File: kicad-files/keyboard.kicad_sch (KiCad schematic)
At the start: 188 parts, among them J1 TYPE-C-31-M12_13, Q1 2N7002, Q2 2N7002, SW1 K2-1187SQ-A4SW-06, T1 53261-0471, T2 53261-0471, U1 STM32F411CEU6, U2 USBLC6-2SC6, U3 AT24C256C-SSHL-T, U4 SGM2007-3.3XN5/TR, Y1 TAXM8M4RFDCET2T

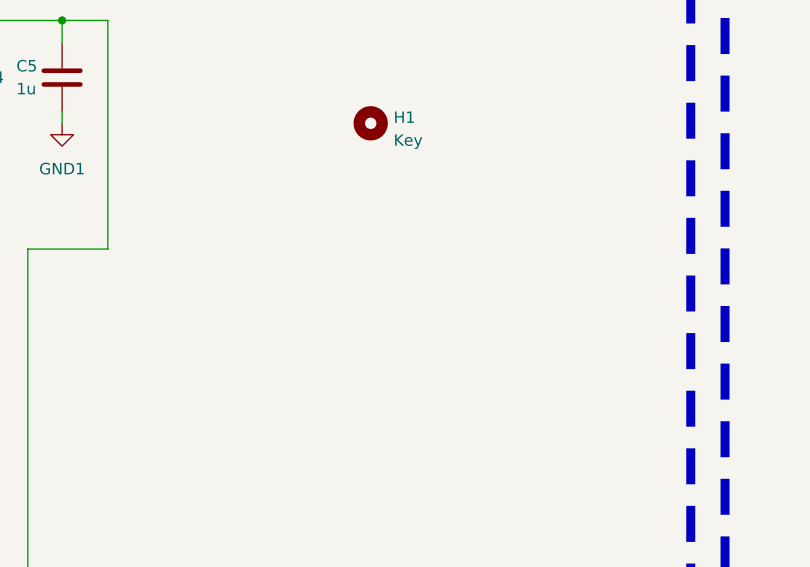
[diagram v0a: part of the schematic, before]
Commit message: Added legshark logo back
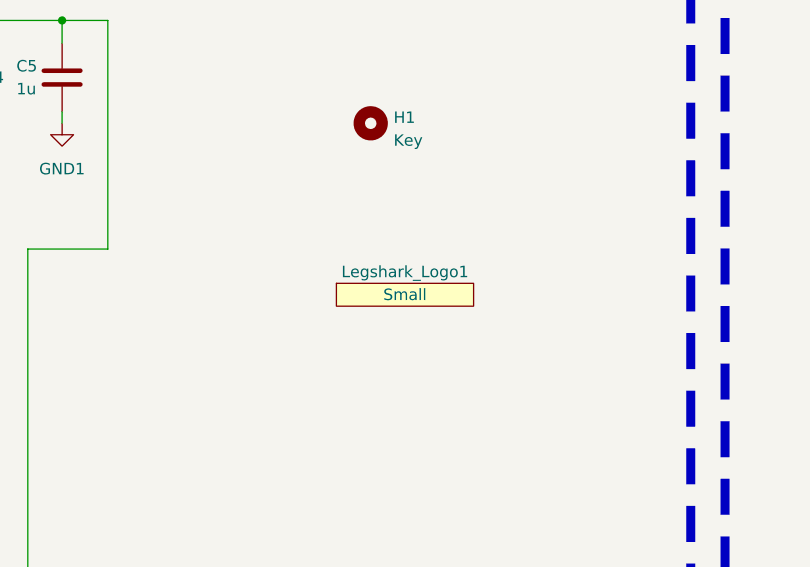
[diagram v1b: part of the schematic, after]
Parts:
- added Legshark_Logo1: Small, Legshark:Legshark_Logo_SMall, symbol legshark_symbols:Legshark_Logo
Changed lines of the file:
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@@
+    )
+  )
+  (symbol (lib_id "legshark_symbols:Legshark_Logo") (at 369.57 345.44 0) (unit 1)
+    (in_bom yes) (on_board yes) (dnp no) (fields_autoplaced)
+    (property "Reference" "Legshark_Logo1" (at 369.57 342.9 0)
+      (effects (font (size 1.27 1.27)))
+    )
+    (property "Value" "Small" (at 369.57 345.44 0)
+      (effects (font (size 1.27 1.27)))
+    )
+    (property "Footprint" "Legshark:Legshark_Logo_SMall" (at 369.57 345.44 0)
+      (effects (font (size 1.27 1.27)) hide)
+    )
+    (property "Datasheet" "" (at 369.57 345.44 0)
+      (effects (font (size 1.27 1.27)) hide)
+    )
+    (instances
+      (project "keyboard"
+        (path "/2fda2561-53ed-4930-8b41-858e0e3dd5f4"
+          (reference "Legshark_Logo1") (unit 1)
+        )
+      )
     )
   )

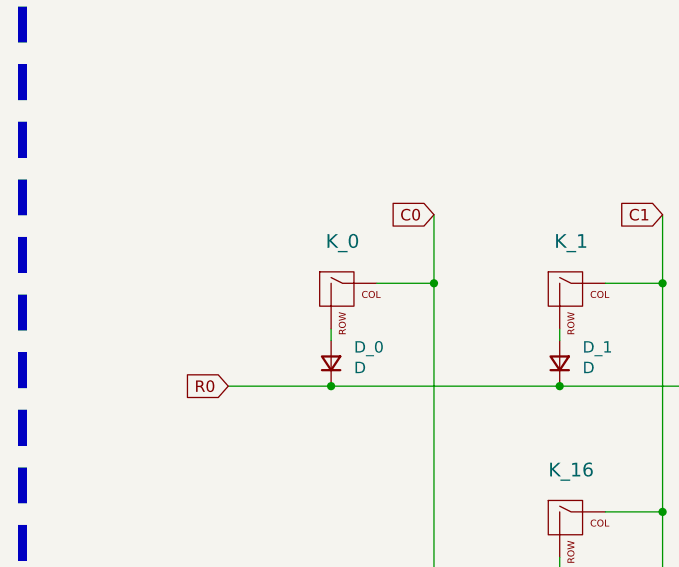
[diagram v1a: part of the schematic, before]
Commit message: Started naming the switches
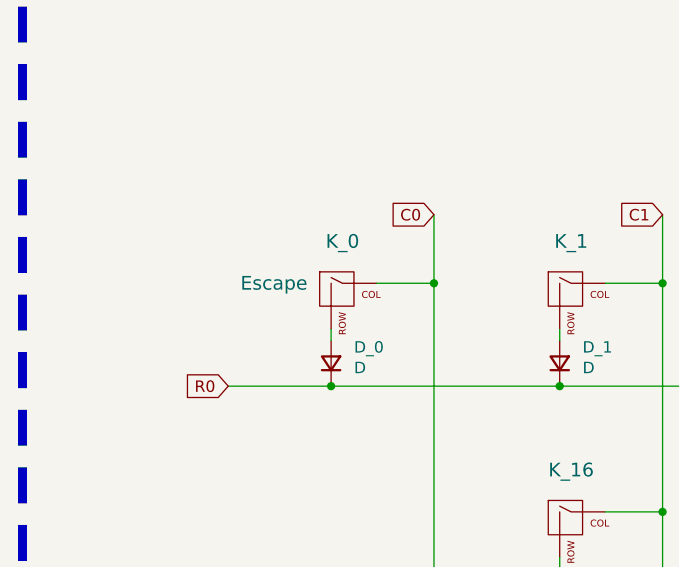
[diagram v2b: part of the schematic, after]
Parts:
- K_0: value KEYSW -> Escape
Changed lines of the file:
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@@
       (effects (font (size 1.524 1.524)))
     )
-    (property "Value" "KEYSW" (at 224.79 146.05 0)
-      (effects (font (size 1.524 1.524)) hide)
+    (property "Value" "Escape" (at 217.17 142.24 0)
+      (effects (font (size 1.524 1.524)))
     )
     (property "Footprint" "MX_Only:MXOnly-1U-NoLED" (at 224.79 143.51 0)

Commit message: Connected all of the columns
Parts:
- added C14: 100n, Capacitor_SMD:C_0603_1608Metric_Pad1.08x0.95mm_HandSolder, symbol Device:C
- added C15: 4.7u, Capacitor_SMD:C_0603_1608Metric_Pad1.08x0.95mm_HandSolder, symbol Device:C
- added C16: 16V 10uF Tantallum, acheron_Components:CP_EIA-3216-10_Kemet-I_Pad1.58x1.35mm_HandSolder, symbol Device:C_Polarized_US
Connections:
- net 3V3: now also U1.1 (VBAT), C14.1, C16.1
- net C0: now also U1.46 (PB9)
- net C1: now also U1.45 (PB8)
- net C10: now also U1.28 (PB15/SPI2_MOSI)
- net C11: now also U1.27 (PB14)
- net C12: now also U1.26 (PB13/SPI2_SCK)
- net C13: now also U1.25 (PB12)
- net C14: now also U1.21 (PB10)
- net C15: now also U1.19 (PB1)
- net C16: now also U1.18 (PB0)
- net C2: now also U1.41 (PB5)
- net C3: now also U1.40 (PB4)
- net C4: now also U1.39 (PB3)
- net C5: now also U1.38 (PA15)
- net C6: now also U1.37 (SWCLK/PA14)
- net C7: now also U1.34 (SWDIO/PA13)
- net C8: now also U1.31 (PA10)
- net C9: now also U1.29 (PA8)
- net GND: now also C14.2, C15.2, C16.2
- net at U1.22 (VCAP_1): now also C15.1
- no-connect marks 2 -> 3
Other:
- note added: "Scary pin that is internally pulled down"

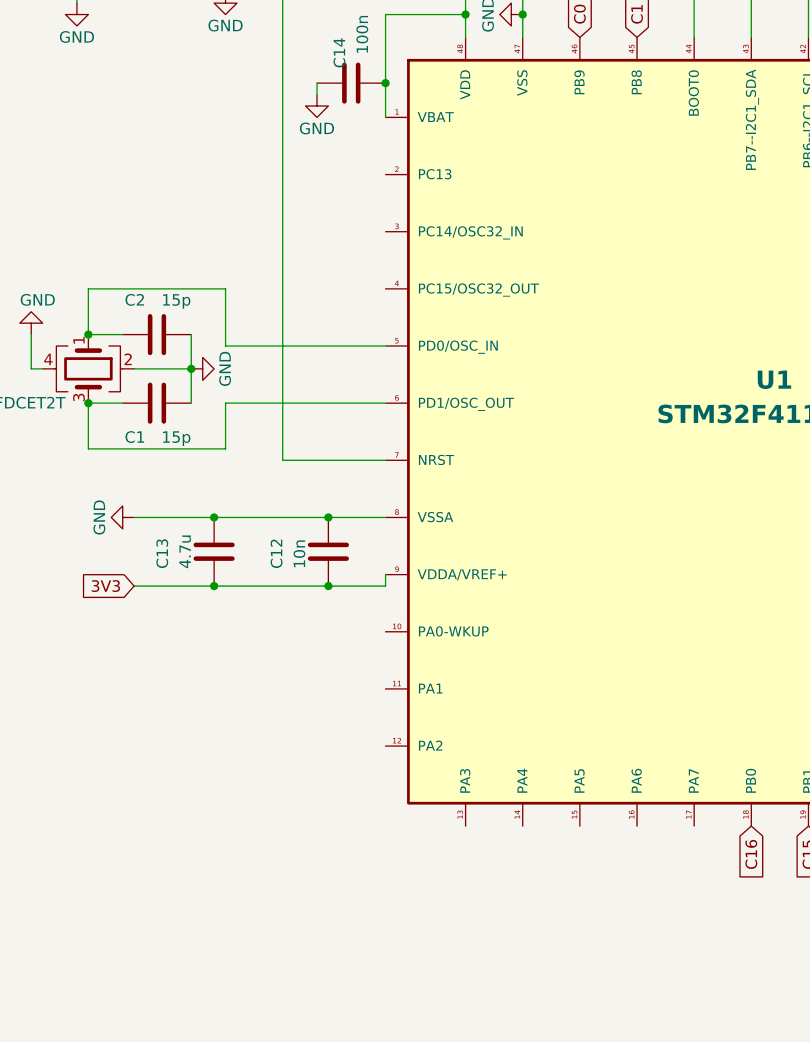
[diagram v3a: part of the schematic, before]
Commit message: Connected all the rows
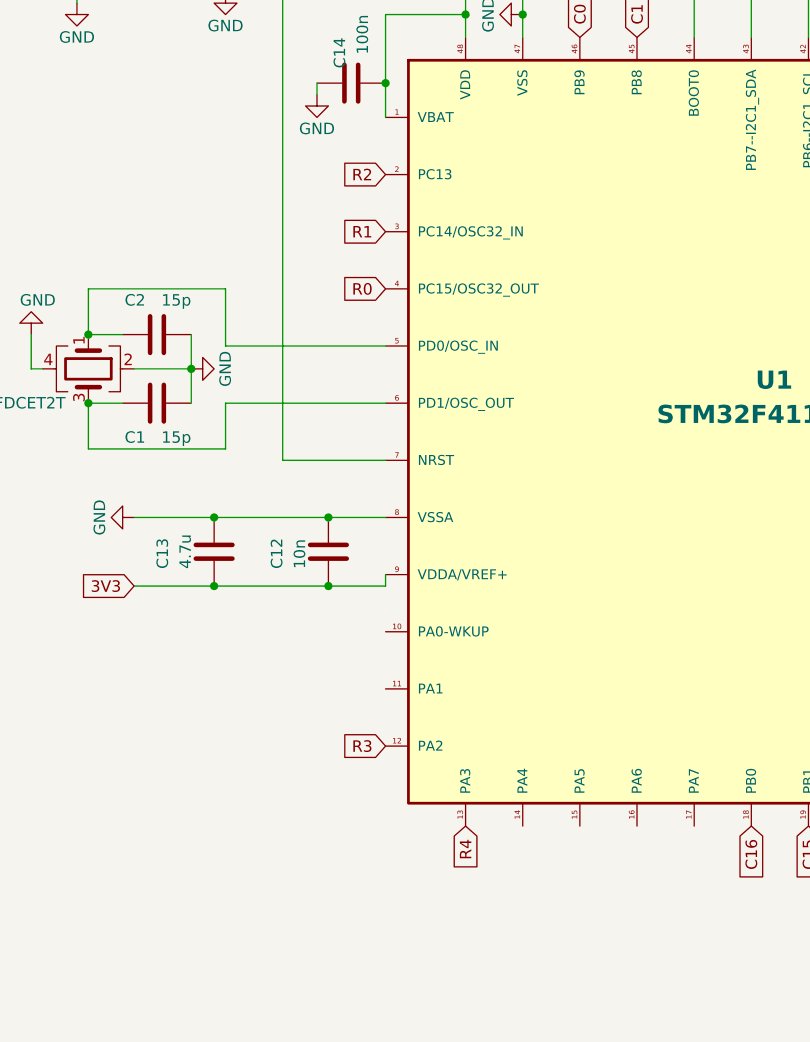
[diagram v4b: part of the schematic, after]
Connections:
- net R0: now also U1.4 (PC15/OSC32_OUT)
- net R1: now also U1.3 (PC14/OSC32_IN)
- net R2: now also U1.2 (PC13)
- net R3: now also U1.12 (PA2)
- net R4: now also U1.13 (PA3)
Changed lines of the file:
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@@
+    )
+  )
+  (global_label "R0" (shape input) (at 504.19 370.84 180) (fields_autoplaced)
+    (effects (font (size 1.27 1.27)) (justify right))
+    (property "Intersheetrefs" "${INTERSHEET_REFS}" (at 499.4589 370.84 0)
+      (effects (font (size 1.27 1.27)) (justify right) hide)
     )
   )
@@
     )
   )
+  (global_label "R1" (shape input) (at 504.19 364.49 180) (fields_autoplaced)
+    (effects (font (size 1.27 1.27)) (justify right))
+    (property "Intersheetrefs" "${INTERSHEET_REFS}" (at 499.4589 364.49 0)
+      (effects (font (size 1.27 1.27)) (justify right) hide)
+    )
+  )
   (global_label "C1" (shape input) (at 532.13 342.9 90) (fields_autoplaced)
     (effects (font (size 1.27 1.27)) (justify left))
@@
     )
   )
+  (global_label "R2" (shape input) (at 504.19 358.14 180) (fields_autoplaced)
+    (effects (font (size 1.27 1.27)) (justify right))
+    (property "Intersheetrefs" "${INTERSHEET_REFS}" (at 499.4589 358.14 0)
+      (effects (font (size 1.27 1.27)) (justify right) hide)
+    )
+  )
+  (global_label "R3" (shape input) (at 504.19 421.64 180) (fields_autoplaced)
+    (effects (font (size 1.27 1.27)) (justify right))
+    (property "Intersheetrefs" "${INTERSHEET_REFS}" (at 499.4589 421.64 0)
+      (effects (font (size 1.27 1.27)) (justify right) hide)
+    )
+  )
   (global_label "C11" (shape input) (at 514.35 134.62 180)
     (effects (font (size 1.27 1.27)) (justify right))
@@
     )
   )
+  (global_label "R4" (shape input) (at 513.08 430.53 270) (fields_autoplaced)
+    (effects (font (size 1.27 1.27)) (justify right))
+    (property "Intersheetrefs" "${INTERSHEET_REFS}" (at 513.08 435.2611 90)
+      (effects (font (size 1.27 1.27)) (justify right) hide)
+    )
+  )

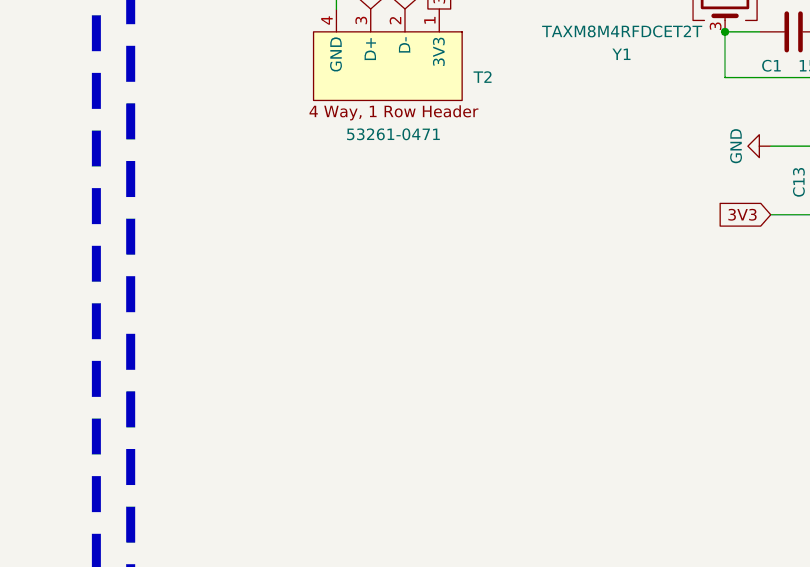
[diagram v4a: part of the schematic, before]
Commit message: Moved some things around a little and added teardrops
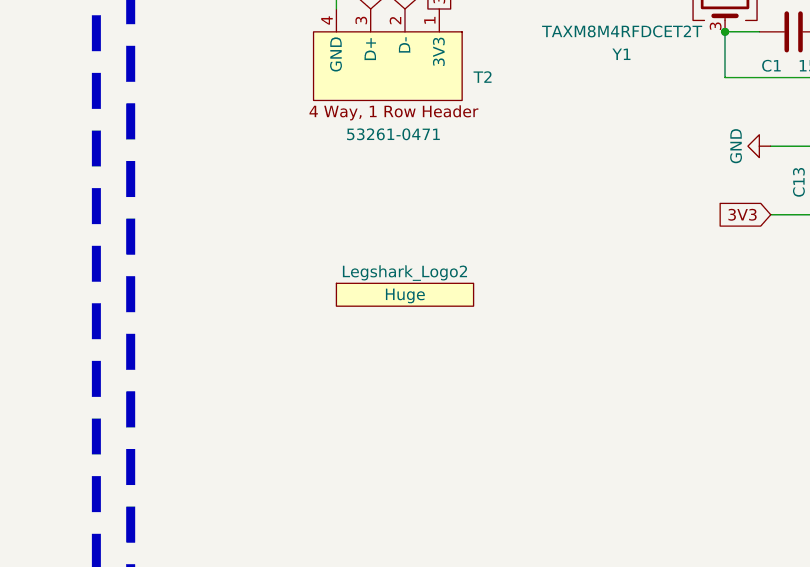
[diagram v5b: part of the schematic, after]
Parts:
- added Legshark_Logo2: Huge, Legshark:Legshark_Logo_Huge, symbol legshark_symbols:Legshark_Logo
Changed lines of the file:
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@@
+    )
+  )
+  (symbol (lib_id "legshark_symbols:Legshark_Logo") (at 435.61 412.75 0) (unit 1)
+    (in_bom yes) (on_board yes) (dnp no)
+    (property "Reference" "Legshark_Logo2" (at 435.61 410.21 0)
+      (effects (font (size 1.27 1.27)))
+    )
+    (property "Value" "Huge" (at 435.61 412.75 0)
+      (effects (font (size 1.27 1.27)))
+    )
+    (property "Footprint" "Legshark:Legshark_Logo_Huge" (at 435.61 412.75 0)
+      (effects (font (size 1.27 1.27)) hide)
+    )
+    (property "Datasheet" "" (at 435.61 412.75 0)
+      (effects (font (size 1.27 1.27)) hide)
+    )
+    (instances
+      (project "keyboard"
+        (path "/2fda2561-53ed-4930-8b41-858e0e3dd5f4"
+          (reference "Legshark_Logo2") (unit 1)
+        )
+      )
     )
   )

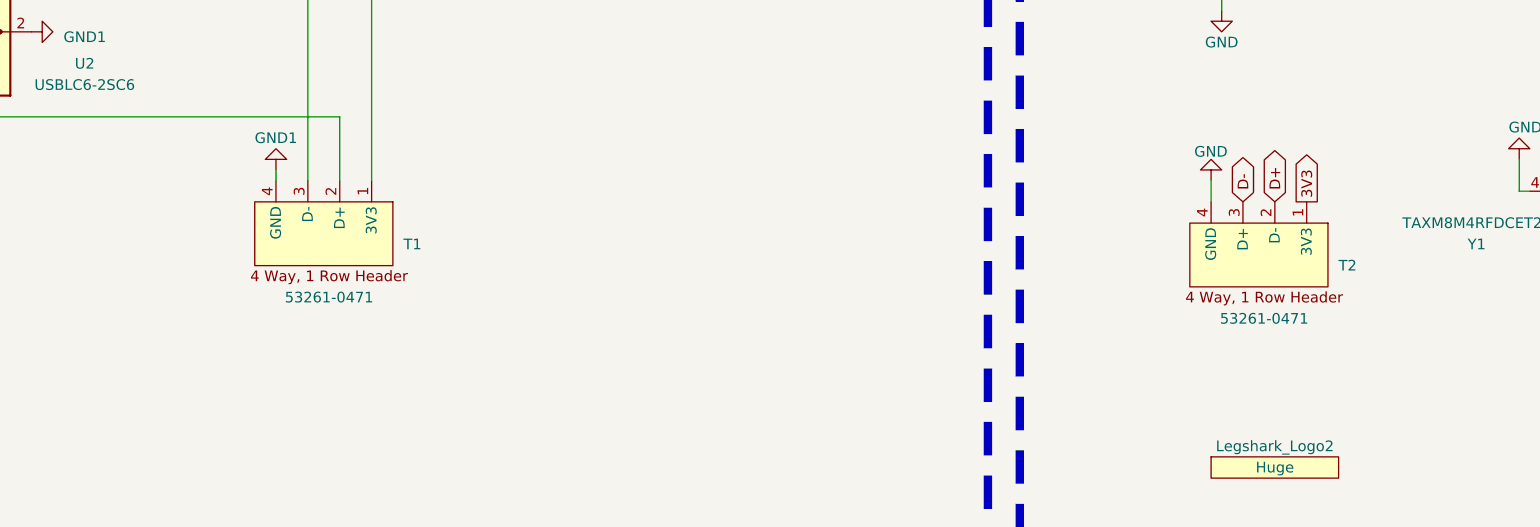
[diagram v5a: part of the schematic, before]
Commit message: Added GND pad to the molex connector
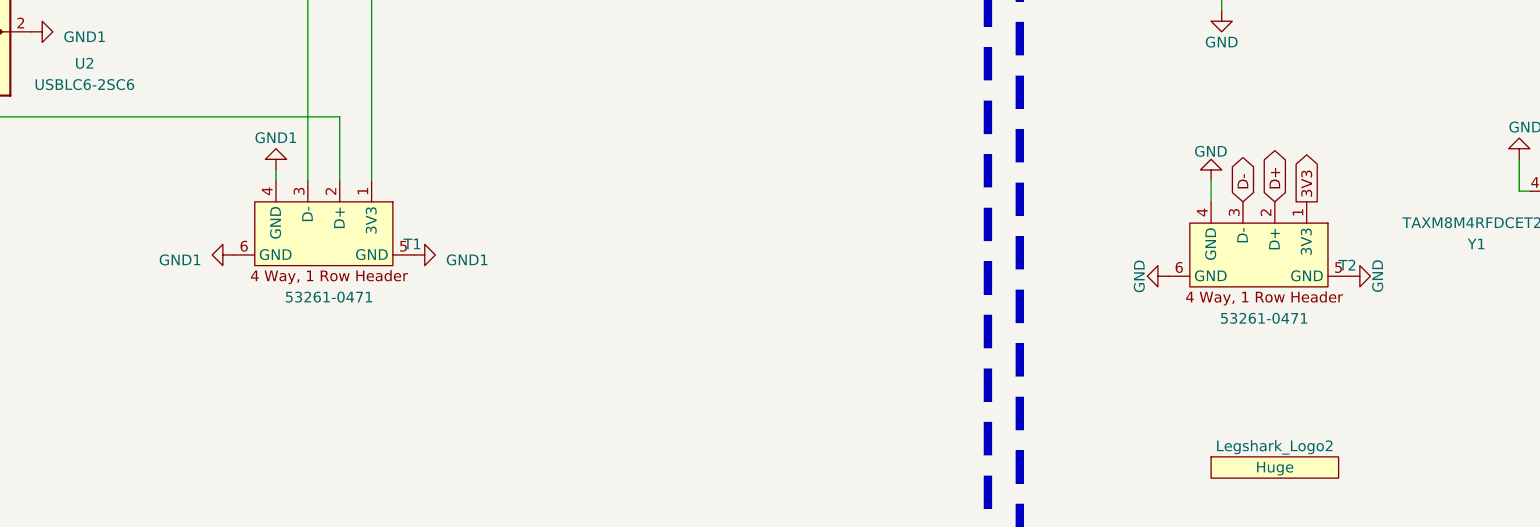
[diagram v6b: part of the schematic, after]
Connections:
- net GND: now also T2.5 (GND), T2.6 (GND)
- net GND1: now also T1.5 (GND), T1.6 (GND)
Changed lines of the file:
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@@
       (effects (font (size 1.27 1.27)) hide)
     )
+    (pin "5")
+    (pin "6")
     (pin "1")
     (pin "2")
@@
     )
   )
+  (symbol (lib_id "power:GND") (at 422.91 389.89 270) (unit 1)
+    (in_bom yes) (on_board yes) (dnp no)
+    (property "Reference" "#PWR037" (at 416.56 389.89 0)
+      (effects (font (size 1.27 1.27)) hide)
+    )
+    (property "Value" "GND" (at 419.4603 391.9046 0)
+      (effects (font (size 1.27 1.27)) (justify right))
+    )
+    (property "Footprint" "" (at 422.91 389.89 0)
+      (effects (font (size 1.27 1.27)) hide)
+    )
+    (property "Datasheet" "" (at 422.91 389.89 0)
+      (effects (font (size 1.27 1.27)) hide)
+    )
+    (pin "1")
+    (instances
+      (project "keyboard"
+        (path "/2fda2561-53ed-4930-8b41-858e0e3dd5f4"
+          (reference "#PWR037") (unit 1)
+        )
+      )
+    )
+  )
   (symbol (lib_id "Device:D_Small") (at 502.92 151.13 90) (unit 1)
     (in_bom yes) (on_board yes) (dnp no)
@@
     )
   )
+  (symbol (lib_id "power:GND1") (at 332.74 387.35 90) (unit 1)
+    (in_bom yes) (on_board yes) (dnp no) (fields_autoplaced)
+    (property "Reference" "#PWR039" (at 339.09 387.35 0)
+      (effects (font (size 1.27 1.27)) hide)
+    )
+    (property "Value" "GND1" (at 336.55 387.985 90)
+      (effects (font (size 1.27 1.27)) (justify right))
+    )
+    (property "Footprint" "" (at 332.74 387.35 0)
+      (effects (font (size 1.27 1.27)) hide)
+    )
+    (property "Datasheet" "" (at 332.74 387.35 0)
+      (effects (font (size 1.27 1.27)) hide)
+    )
+    (pin "1")
+    (instances
+      (project "keyboard"
+        (path "/2fda2561-53ed-4930-8b41-858e0e3dd5f4"
+          (reference "#PWR039") (unit 1)
+        )
+      )
+    )
+  )
   (symbol (lib_id "Device:D_Small") (at 299.72 201.93 90) (unit 1)
     (in_bom yes) (on_board yes) (dnp no)
@@
     )
   )
+  (symbol (lib_id "power:GND") (at 444.5 389.89 90) (unit 1)
+    (in_bom yes) (on_board yes) (dnp no)
+    (property "Reference" "#PWR036" (at 450.85 389.89 0)
+      (effects (font (size 1.27 1.27)) hide)
+    )
+    (property "Value" "GND" (at 447.9497 387.8754 0)
+      (effects (font (size 1.27 1.27)) (justify right))
+    )
+    (property "Footprint" "" (at 444.5 389.89 0)
+      (effects (font (size 1.27 1.27)) hide)
+    )
+    (property "Datasheet" "" (at 444.5 389.89 0)
+      (effects (font (size 1.27 1.27)) hide)
+    )
+    (pin "1")
+    (instances
+      (project "keyboard"
+        (path "/2fda2561-53ed-4930-8b41-858e0e3dd5f4"
+          (reference "#PWR036") (unit 1)
+        )
+      )
+    )
+  )
   (symbol (lib_id "MX_Alps_Hybrid:MX-NoLED") (at 631.19 143.51 0) (unit 1)
     (in_bom yes) (on_board yes) (dnp no)
@@
     )
   )
+  (symbol (lib_id "power:GND1") (at 311.15 387.35 270) (unit 1)
+    (in_bom yes) (on_board yes) (dnp no) (fields_autoplaced)
+    (property "Reference" "#PWR038" (at 304.8 387.35 0)
+      (effects (font (size 1.27 1.27)) hide)
+    )
+    (property "Value" "GND1" (at 307.34 387.985 90)
+      (effects (font (size 1.27 1.27)) (justify right))
+    )
+    (property "Footprint" "" (at 311.15 387.35 0)
+      (effects (font (size 1.27 1.27)) hide)
+    )
+    (property "Datasheet" "" (at 311.15 387.35 0)
+      (effects (font (size 1.27 1.27)) hide)
+    )
+    (pin "1")
+    (instances
+      (project "keyboard"
+        (path "/2fda2561-53ed-4930-8b41-858e0e3dd5f4"
+          (reference "#PWR038") (unit 1)
+        )
+      )
+    )
+  )
   (symbol (lib_id "MX_Alps_Hybrid:MX-NoLED") (at 631.19 245.11 0) (unit 1)
     (in_bom yes) (on_board yes) (dnp no)
@@
       (effects (font (size 1.27 1.27)) hide)
     )
+    (pin "5")
+    (pin "6")
     (pin "1")
     (pin "2")
